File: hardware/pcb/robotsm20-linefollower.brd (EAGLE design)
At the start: 160 x 100 mm, 78 parts, among them IC2 TPS43061RTER, Q1 CSD15571Q2, Q2 CSD15571Q2, U1 STM32F405RG

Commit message: Update
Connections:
- removed net N$28: U$6.2
- net +5V: now also U$6.2
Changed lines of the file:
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@@
 <contactref element="PS1" pad="5"/>
 <contactref element="R5" pad="2"/>
+<contactref element="U$6" pad="2"/>
 <wire x1="120.97" y1="8.89" x2="125.31" y2="10.16" width="0" layer="19" extent="1-1"/>
 <wire x1="120.43" y1="4.105" x2="120.97" y2="8.89" width="0" layer="19" extent="1-1"/>
@@
 <wire x1="19.5326" y1="42.94" x2="118.33" y2="4.105" width="0" layer="19" extent="1-1"/>
 <wire x1="17.46" y1="45.72" x2="19.5326" y2="42.94" width="0" layer="19" extent="1-1"/>
+<wire x1="-72.39" y1="-234.95" x2="19.5326" y2="42.94" width="0" layer="19" extent="1-1"/>
 </signal>
 <signal name="N$3">
@@
 <wire x1="-50.38" y1="-245.11" x2="-52.07" y2="-241.3" width="0" layer="19" extent="1-1"/>
 </signal>
-<signal name="N$28">
-<contactref element="U$6" pad="2"/>
-</signal>
 </signals>

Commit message: Motor driver finished except for ROSC
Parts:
- added C41: 270pF, rcl:C0805
- added R21: (no value), rcl:R0603
- added R22: 19.4k, rcl:R0603
- added R23: 10k, rcl:R0603
- added R24, R25: R001, rcl:R2512W
- moved C30 220.7 mm to (-97.8, 102.9), turned to 90 degrees
- moved C29 205.3 mm to (-88.9, 101.6), turned to 90 degrees
- moved C28 196.4 mm to (-72.4, 73.7)
- moved C27 187.9 mm to (-66.0, 77.5)
- moved C22 167.1 mm to (-74.9, 94.0)
- moved C23 167.1 mm to (-74.9, 87.6)
- moved R11 167.1 mm to (-74.9, 109.2)
- moved R12 167.1 mm to (-74.9, 105.4)
- moved R13 167.1 mm to (-73.7, 99.1)
- moved R16 166.8 mm to (-43.2, 73.7)
- moved C25 165.1 mm to (-16.5, 97.8), turned to 90 degrees
- moved C24 163.8 mm to (-25.4, 97.8), turned to 90 degrees
- moved C26 163.2 mm to (-40.6, 76.2)
- moved R15 156.6 mm to (-31.8, 73.7)
- moved U$3 156.4 mm to (-57.1, 92.7)
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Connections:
- net LO1,5V renamed LO1
- net LO2,5V renamed LO2
- removed net CUR-IN1+: U$5.3
- removed net CUR-IN1-: U$5.2
- removed net CUR-IN2+: U$5.7
- removed net CUR-IN2-: U$5.8
- removed net RSAGND: U$1.15, U$1.16
- removed net RSBGND: U$1.21, U$1.22
- new net MOTORA+: R24.2, U$5.2
- new net MOTORA+_HIGH: R24.1, U$1.13, U$1.14, U$5.3
- new net MOTORA-: U$1.17, U$1.18
- new net MOTORB+: R25.2, U$5.8
- new net MOTORB+_HIGH: R25.1, U$1.23, U$1.24, U$5.7
- new net MOTORB-: U$1.19, U$1.20
- new net N$28: R22.2, R23.1, U$1.31, U$1.32
- new net N$29: C41.1, R21.2, R23.2, U$1.33, U$1.34
- new net N$31: R21.1, U$1.35
- net GND: now also C41.2, R22.1, U$1.15, U$1.16, U$1.21, U$1.22
- net VCC: no longer U$1.33, U$1.34

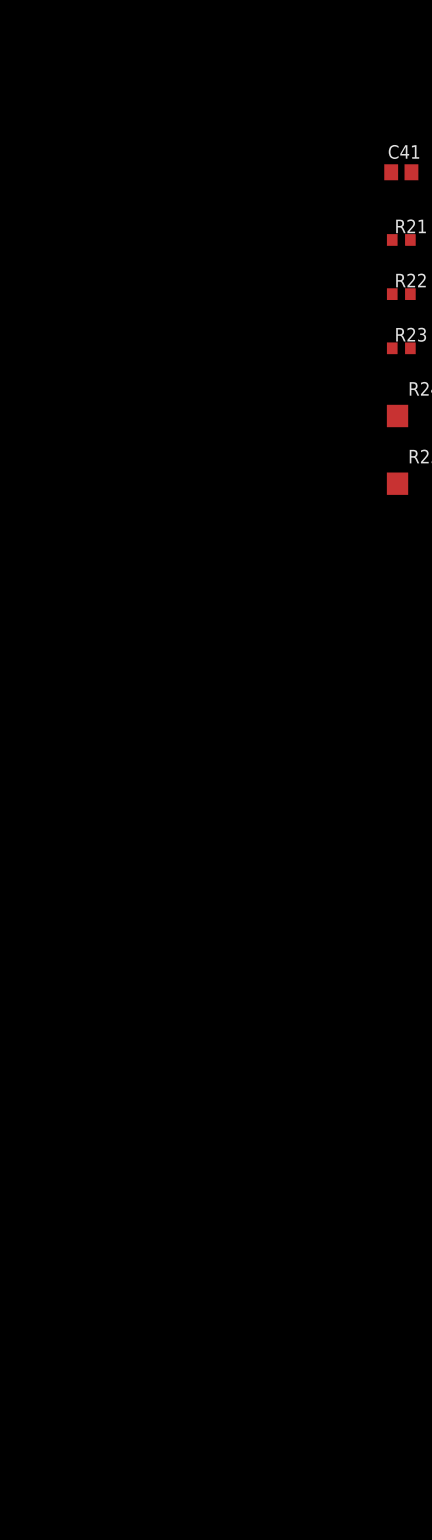
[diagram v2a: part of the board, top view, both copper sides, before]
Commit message: Added IMU, Battery switch, BT,
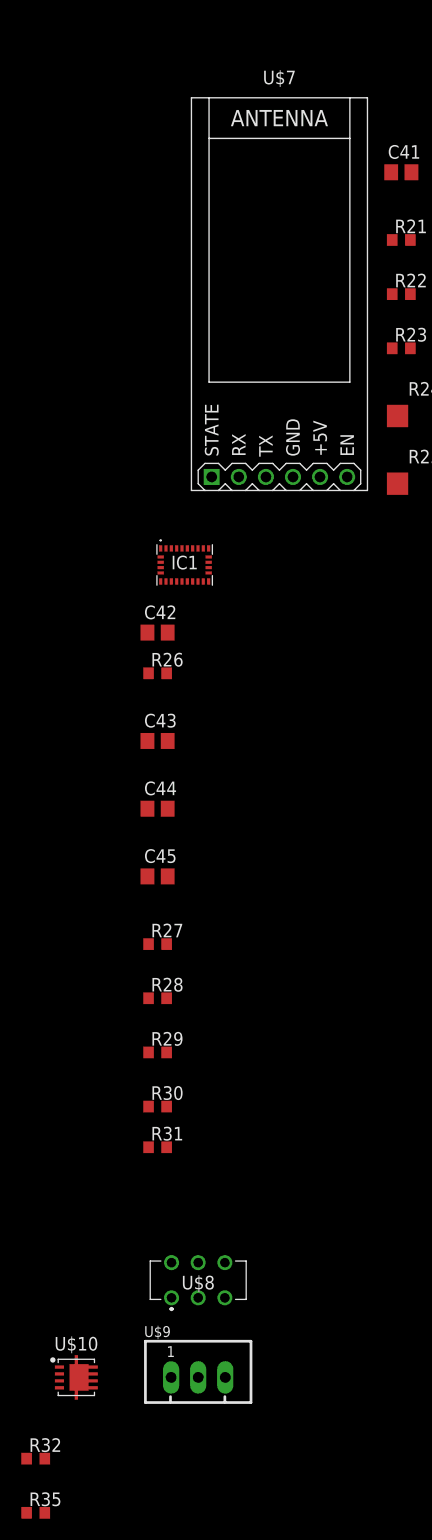
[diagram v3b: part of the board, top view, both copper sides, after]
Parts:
- added C42: (no value), rcl:C0805
- added C43: 100nF, rcl:C0805
- added C44: 120nF, rcl:C0805
- added C45: 6.8nF, rcl:C0805
- added IC1: BNO055, Sensors:BNO055
- added R26, R27, R28, R29, R30, R31, R32, R35: 10k, rcl:R0603
- added U$10: DMP2010UFV, PowerManagement:POWERDI3333-8
- added U$7: WIRELESS-BLUETOOTH-HC-05, Isaks Bibliotek:WIRELESS-BLUETOOTH-HC-05
- added U$8: JS202011AQN, Switches:JS202011AQN
- added U$9: JST-XH-03, Isaks Bibliotek:JST-XH-03
- R17, R18, R19, R20: value 10k -> (none)
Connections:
- new net IMU_INT: IC1.14
- new net N$27: IC1.11, R27.1
- new net N$30: C42.1, IC1.9
- new net N$36: C43.1
- new net N$37: IC1.4, R26.1
- new net N$38: U$10.1, U$10.2, U$10.3, U$9.3
- new net N$39: IC1.17, R28.2, R29.1
- new net N$40: R32.1, U$10.4, U$8.2, U$8.5
- new net N$42: R35.1, U$8.1, U$8.4
- net +3V3: now also C44.1, C45.1, IC1.28, IC1.3, R26.2, R27.2, R29.2
- net +5V: now also U$7.5
- net 3.3V: now also R30.1, R31.1
- net AGND: now also C42.2, C43.2, C44.2, C45.2, IC1.10, IC1.15, IC1.16, IC1.18, IC1.2, IC1.25, IC1.5, IC1.6, R28.1
- net GND: now also U$7.4, U$8.3, U$8.6, U$9.1
- net RX_BT: now also U$7.3
- net SCL: now also IC1.19, R31.2
- net SDA: now also IC1.20, R30.2
- net TX_BT: now also U$7.2
- net V+: now also R32.2, R35.2, U$10.10, U$10.11, U$10.5, U$10.6, U$10.7, U$10.8, U$10.9

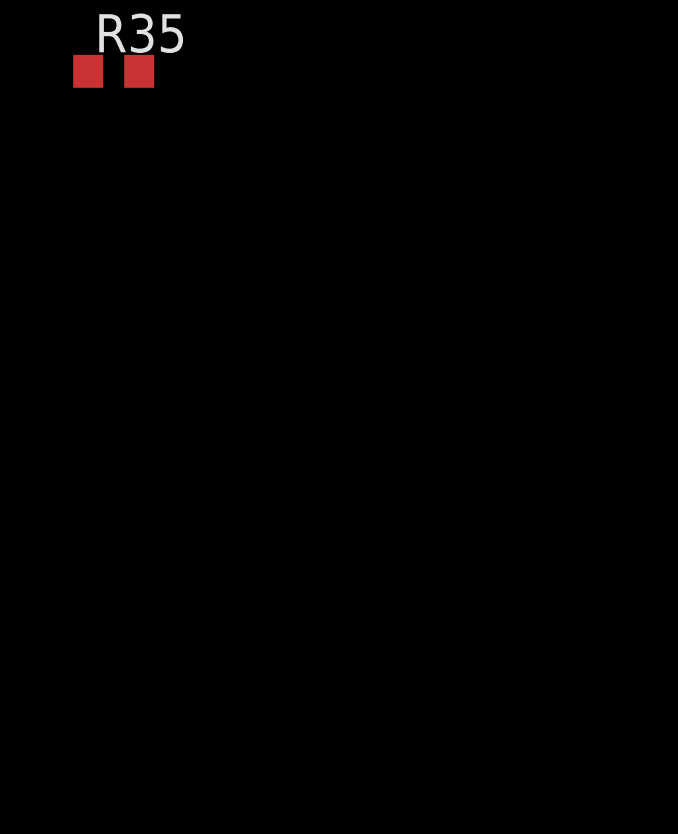
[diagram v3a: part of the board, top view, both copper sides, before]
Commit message: Added interface button
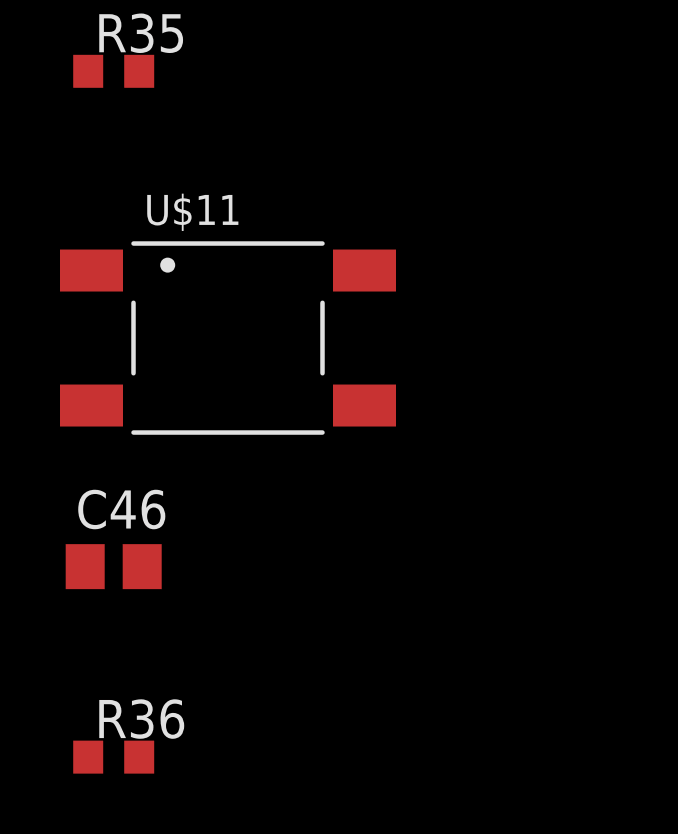
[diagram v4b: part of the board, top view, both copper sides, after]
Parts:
- added C46: 0.1u, rcl:C0805
- added R36: 10k, rcl:R0603
- added U$11: TSM2JSMA, CASE-Switches:TSM2JSMA
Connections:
- new net INTERFACE_BUT1: R36.1
- net +3V3: now also C46.1, R36.2, U$11.1, U$11.2
- net GND: now also C46.2, U$11.3, U$11.4
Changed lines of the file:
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@@
 <attribute name="VALUE" x="-136.525" y="-396.875" size="1.27" layer="27"/>
+</element>
+<element name="U$11" library="CASE-Switches" library_urn="urn:adsk.eagle:library:7770839" package="TSM2JSMA" package3d_urn="urn:adsk.eagle:package:17798453/2" value="TSM2JSMA" x="-132.08" y="-403.86" smashed="yes">
+<attribute name="NAME" x="-134.88" y="-400.09" size="1" layer="25"/>
+</element>
+<element name="C46" library="rcl" library_urn="urn:adsk.eagle:library:334" package="C0805" package3d_urn="urn:adsk.eagle:package:23617/2" value="0.1u" x="-135.89" y="-411.48" smashed="yes">
+<attribute name="NAME" x="-137.16" y="-410.21" size="1.27" layer="25"/>
+<attribute name="POPULARITY" value="88" x="-135.89" y="-411.48" size="1.778" layer="27" display="off"/>
+<attribute name="SPICEPREFIX" value="C" x="-135.89" y="-411.48" size="1.778" layer="27" display="off"/>
+<attribute name="VALUE" x="-137.16" y="-414.02" size="1.27" layer="27"/>
+</element>
+<element name="R36" library="rcl" library_urn="urn:adsk.eagle:library:334" package="R0603" package3d_urn="urn:adsk.eagle:package:23555/3" value="10k" x="-135.89" y="-417.83" smashed="yes">
+<attribute name="NAME" x="-136.525" y="-417.195" size="1.27" layer="25"/>
+<attribute name="POPULARITY" value="70" x="-135.89" y="-417.83" size="1.778" layer="27" display="off"/>
+<attribute name="SPICEPREFIX" value="R" x="-135.89" y="-417.83" size="1.778" layer="27" display="off"/>
+<attribute name="VALUE" x="-136.525" y="-419.735" size="1.27" layer="27"/>
 </element>
 </elements>
@@
 <contactref element="U$8" pad="3"/>
 <contactref element="U$8" pad="6"/>
+<contactref element="C46" pad="2"/>
+<contactref element="U$11" pad="3"/>
+<contactref element="U$11" pad="4"/>
 <wire x1="-118.15" y1="-374.805" x2="-123.19" y2="-382.27" width="0" layer="19" extent="1-1"/>
 <wire x1="-118.15" y1="-371.505" x2="-118.15" y2="-374.805" width="0" layer="19" extent="1-1"/>
+<wire x1="-127.53" y1="-406.11" x2="-123.19" y2="-382.27" width="0" layer="19" extent="1-1"/>
+<wire x1="-136.63" y1="-406.11" x2="-127.53" y2="-406.11" width="0" layer="19" extent="1-1"/>
+<wire x1="-134.94" y1="-411.48" x2="-136.63" y2="-406.11" width="0" layer="19" extent="1-1"/>
 <wire x1="-111.76" y1="-297.815" x2="-118.15" y2="-371.505" width="0" layer="19" extent="1-1"/>
 <wire x1="-102.45" y1="-280.67" x2="-111.76" y2="-297.815" width="0" layer="19" extent="1-1"/>
@@
 <contactref element="R27" pad="2"/>
 <contactref element="R29" pad="2"/>
+<contactref element="U$11" pad="2"/>
+<contactref element="U$11" pad="1"/>
+<contactref element="C46" pad="1"/>
+<contactref element="R36" pad="2"/>
 <wire x1="-123.61" y1="-341.63" x2="-123.61" y2="-351.79" width="0" layer="19" extent="1-1"/>
 <wire x1="-125.41" y1="-335.28" x2="-123.61" y2="-341.63" width="0" layer="19" extent="1-1"/>
@@
 <wire x1="-124.17" y1="-305.82" x2="-123.61" y2="-316.23" width="0" layer="19" extent="1-1"/>
 <wire x1="-123.67" y1="-304.52" x2="-124.17" y2="-305.82" width="0" layer="19" extent="1-1"/>
+<wire x1="-127.53" y1="-401.61" x2="-123.61" y2="-351.79" width="0" layer="19" extent="1-1"/>
+<wire x1="-136.63" y1="-401.61" x2="-127.53" y2="-401.61" width="0" layer="19" extent="1-1"/>
+<wire x1="-136.84" y1="-411.48" x2="-136.63" y2="-401.61" width="0" layer="19" extent="1-1"/>
+<wire x1="-135.04" y1="-417.83" x2="-136.84" y2="-411.48" width="0" layer="19" extent="1-1"/>
 <wire x1="15.56" y1="35.56" x2="-123.67" y2="-304.52" width="0" layer="19" extent="1-1"/>
 <wire x1="13.4874" y1="40.64" x2="15.56" y2="35.56" width="0" layer="19" extent="1-1"/>
@@
 <wire x1="-136.74" y1="-394.97" x2="-123.15" y2="-374.805" width="0" layer="19" extent="1-1"/>
 </signal>
+<signal name="INTERFACE_BUT1">
+<contactref element="R36" pad="1"/>
+</signal>
 </signals>

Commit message: Added rgb led, xt30 for battery and changed to nmosfet
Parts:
- removed U$10: DMP2010UFV, PowerManagement:POWERDI3333-8
- removed U$8: JS202011AQN, Switches:JS202011AQN
- removed U$9: JST-XH-03, Isaks Bibliotek:JST-XH-03
- added D1: CHIP-LED0805, CASE-LED:CHIP-LED0805
- added ENC_L, ENC_R: ZR_B6B-ZR, CASE-JST:B6B-ZR
- added LED1: 150141M173100, CASE-LED:150141M173100
- added MOTOR_L, MOTOR_R: EH_B2B-EH, CASE-JST:B2B-EH
- added Q3, Q4: CSD15571Q2, PowerManagement:TRANS_CSD15571Q2
- added Q5, Q6, Q7: BSS138LT3G, CASE-Transistors:SOT23
- added R37: 100R, rcl:R0603
- added R38, R40: 0R, rcl:R0603
- added R39, R41, R42: 10k, rcl:R0603
- added U$15: XT30PW-M, Connectors:XT30PW-M
- added U$16: JS202011AQN, Switches:JS202011AQN
- R32: value 10k -> 245R
- R36: value 10k -> 50R
- moved C46 552.4 mm to (25.4, 116.8), turned to 270 degrees
- moved U$11 546.2 mm to (33.0, 116.8)
- moved R29 333.4 mm to (-26.7, -33.0)
- moved R28 330.9 mm to (-22.9, -31.8)
- moved R27 329.3 mm to (-20.3, -29.2)
- moved C45 325.7 mm to (-20.3, -26.7)
- moved C44 322.1 mm to (-20.3, -24.1)
- moved C43 306.1 mm to (-33.0, -30.5)
- moved R26 302.4 mm to (-33.0, -27.9)
- moved C42 301.2 mm to (-33.0, -25.4)
- moved IC1 295.2 mm to (-26.7, -26.7)
- moved U$7 255.8 mm to (-73.7, -27.9), turned to 90 degrees
- moved U$6 195.6 mm to (-69.8, -52.1), turned to 270 degrees
- moved R36 73.7 mm to (-134.6, -344.2)
- moved R35 57.3 mm to (-123.2, -339.1)
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- renumbered U$1 to MOTORDRIVER, U$5 to CURRENTAMP
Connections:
- net MOTORA+_HIGH renamed MOTOR_L+_HIGH
- net MOTORB+_HIGH renamed MOTOR_R+_HIGH
- removed net INA1: MOTORDRIVER.41
- removed net INA2: MOTORDRIVER.42
- removed net INB1: MOTORDRIVER.43
- removed net INB2: MOTORDRIVER.44
- removed net MOTORA+: CURRENTAMP.2, R24.2
- removed net MOTORA-: MOTORDRIVER.17, MOTORDRIVER.18
- removed net MOTORB+: CURRENTAMP.8, R25.2
- removed net MOTORB-: MOTORDRIVER.19, MOTORDRIVER.20
- removed net N$60: U1.59
- removed net N$62: U1.57
- removed net N$63: U1.58
- removed net N$65: U1.56
- removed net PWMA: MOTORDRIVER.39
- removed net PWMB: MOTORDRIVER.40
- new net 3.3V1: R41.1, R42.1
- new net BAT-: Q3.4, Q3.7, Q4.4, Q4.7, R39.1, U$15.-, U$16.1, U$16.4
- new net ENC_L_I: ENC_L.2
- new net ENC_R_I: ENC_R.2
- new net IN_L_1: MOTORDRIVER.41, U1.56
- new net IN_L_2: MOTORDRIVER.42, U1.57
- new net IN_R_1: MOTORDRIVER.43, U1.58
- new net IN_R_2: MOTORDRIVER.44, U1.59
- new net MOTOR_L+: CURRENTAMP.2, MOTOR_L.1, R24.2
- new net MOTOR_L-: MOTORDRIVER.17, MOTORDRIVER.18, MOTOR_L.2
- new net MOTOR_R+: CURRENTAMP.8, MOTOR_R.1, R25.2
- new net MOTOR_R-: MOTORDRIVER.19, MOTORDRIVER.20, MOTOR_R.2
- new net N$41: Q3.3, Q4.3, R37.1
- new net N$43: LED1.2, R40.2
- new net N$45: Q5.3, R36.1
- new net N$46: Q6.3, R38.1
- new net N$47: R37.2, R39.2, U$16.2, U$16.5
- new net N$48: Q7.3, R40.1
- net +3V3: now also ENC_L.4, ENC_R.4, LED1.1, R1.2, R2.2, R35.2; no longer C46.1, R36.2
- net 3.3V: no longer R1.2, R2.2
- net AGND: now also ENC_L.3, ENC_R.3
- net ENC_L_A: now also ENC_L.6
- net ENC_L_B: now also ENC_L.5
- net ENC_R_A: now also ENC_R.6
- net ENC_R_B: now also ENC_R.5
- net GND: now also Q3.1, Q3.2, Q3.5, Q3.6, Q3.8, Q4.1, Q4.2, Q4.5, Q4.6, Q4.8, Q5.2, Q6.2, Q7.2, R32.1; no longer U$8.3, U$8.6, U$9.1
- net INTERFACE_BUT1: now also C46.1, R35.1; no longer R36.1
- net LED_B: now also Q7.1
- net LED_G: now also Q6.1
- net LED_R: now also Q5.1
- net N$38: now also D1.C, R32.2; no longer U$10.1, U$10.2, U$10.3, U$9.3
- net N$40: now also LED1.3, R36.2; no longer R32.1, U$10.4, U$8.2, U$8.5
- net N$42: now also LED1.4, R38.2; no longer R35.1, U$8.1, U$8.4
- net PWM_L: now also MOTORDRIVER.39
- net PWM_R: now also MOTORDRIVER.40
- net RX: now also R41.2
- net TX: now also R42.2
- net V+: now also D1.A, U$15.+, U$16.3, U$16.6; no longer R32.2, R35.2, U$10.10, U$10.11, U$10.5, U$10.6, U$10.7, U$10.8, U$10.9
